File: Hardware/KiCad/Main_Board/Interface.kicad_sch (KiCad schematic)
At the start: 5 parts, among them J3 Conn_01x11_Pin, SW2 RotaryEncoder_Switch_MP

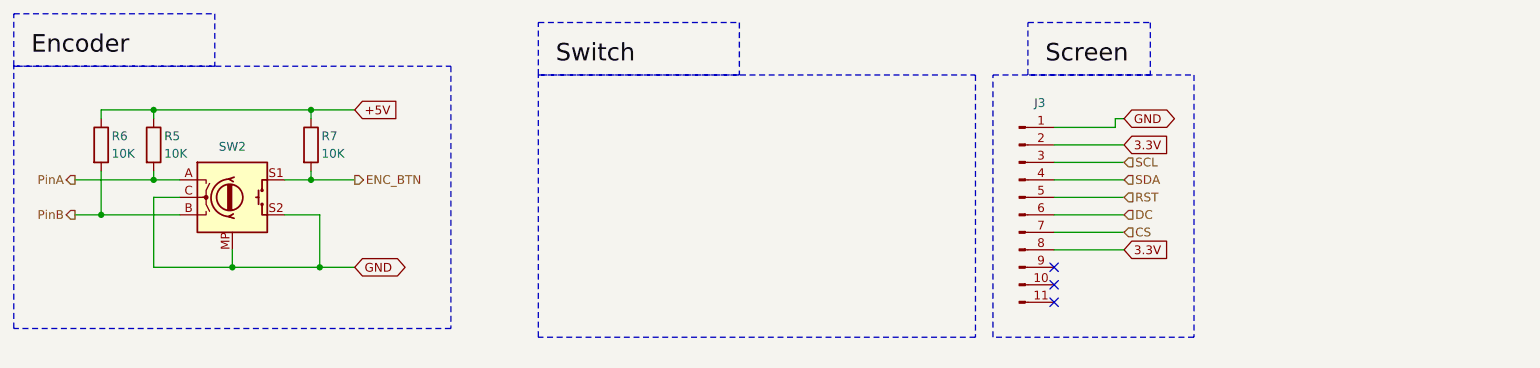
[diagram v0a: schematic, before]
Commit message: Interface hierarchical out for screen and encoder
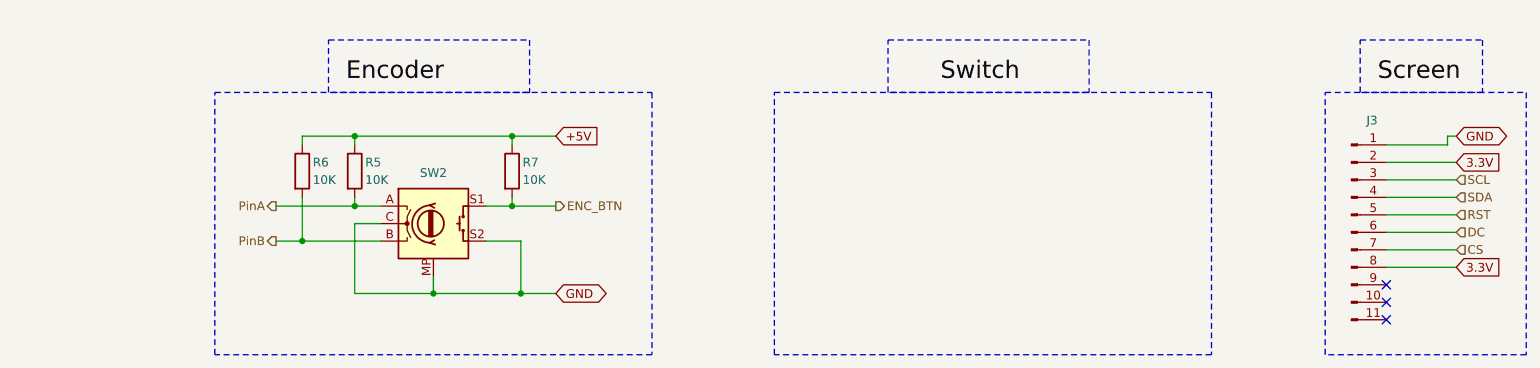
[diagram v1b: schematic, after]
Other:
- moved on the sheet: J3, R5, R6, R7, SW2
